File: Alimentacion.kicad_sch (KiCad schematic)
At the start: 0 parts

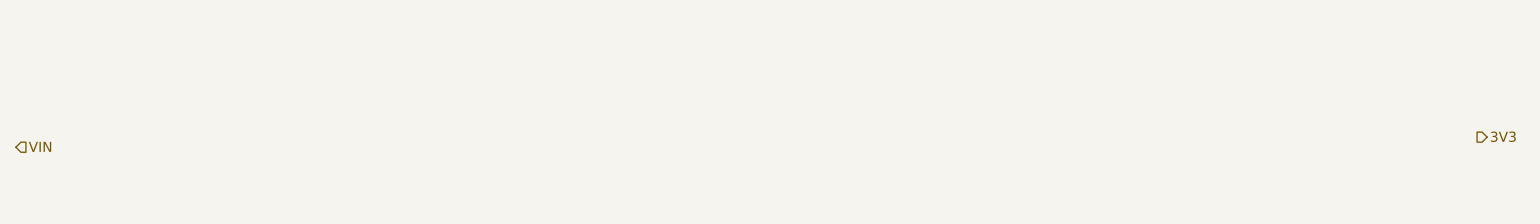
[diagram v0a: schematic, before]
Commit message: Alimentacion: J101 bornas 9 V, U201 MCP1703A 3,3 V, C201/C202 1 uF (huellas y MPN)
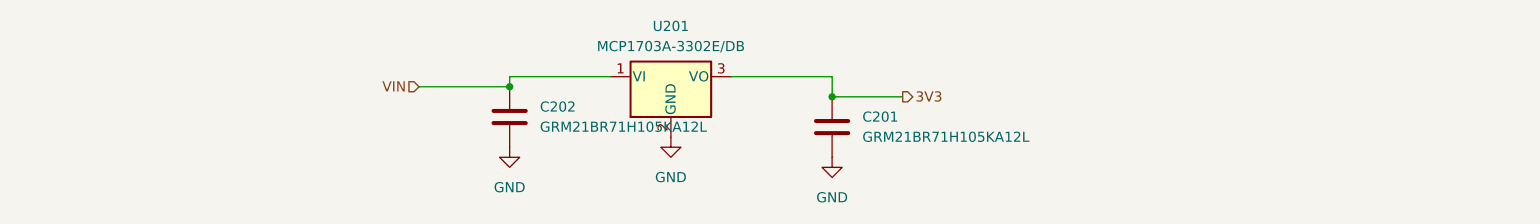
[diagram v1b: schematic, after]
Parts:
- added C201: GRM21BR71H105KA12L, Capacitor_SMD:C_0805_2012Metric_Pad1.18x1.45mm_HandSolder, symbol Device:C
- added C202: GRM21BR71H105KA12L, Package_TO_SOT_SMD:SOT-223-3_TabPin2, symbol Device:C
- added U201: MCP1703A-3302E/DB, Package_TO_SOT_SMD:SOT-223-3_TabPin2, symbol Regulator_Linear:MCP1703Ax-330xxDB
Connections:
- net 3V3: now also C201.1, U201.3 (VO)
- net VIN: now also C202.1, U201.1 (VI)
- new net GND: C201.2, C202.2, U201.2 (GND)

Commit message: Correcciones
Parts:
- C202: footprint Package_TO_SOT_SMD:SOT-223-3_TabPin2 -> Capacitor_SMD:C_0805_2012Metric_Pad1.18x1.45mm_HandSolder
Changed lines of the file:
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@@
 			)
 		)
-		(property "Footprint" "Package_TO_SOT_SMD:SOT-223-3_TabPin2"
+		(property "Footprint" "Capacitor_SMD:C_0805_2012Metric_Pad1.18x1.45mm_HandSolder"
 			(at 112.7252 101.6 0)
 			(hide yes)

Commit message: Correcciones: huella C202, conectores J301/J302, SWD al MCU, MPN en su campo y BOM
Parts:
- C201, C202: MPN (none) -> GRM21BR71H105KA12L; Manufacturer (none) -> Murata
- U201: MPN (none) -> MCP1703A-3302E/DB; Manufacturer (none) -> Microchip
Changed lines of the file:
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@@
 			)
 		)
-		(property "MPN" ""
+		(property "MPN" "MCP1703A-3302E/DB"
 			(at 132.08 92.71 0)
 			(hide yes)
@@
 			)
 		)
-		(property "Manufacturer" ""
+		(property "Manufacturer" "Microchip"
 			(at 132.08 92.71 0)
 			(hide yes)
@@
 			)
 		)
-		(property "MPN" ""
+		(property "MPN" "GRM21BR71H105KA12L"
 			(at 152.4 99.06 0)
 			(hide yes)
@@
 			)
 		)
-		(property "Manufacturer" ""
+		(property "Manufacturer" " Murata"
 			(at 152.4 99.06 0)
 			(hide yes)
@@
 			)
 		)
-		(property "MPN" ""
+		(property "MPN" "GRM21BR71H105KA12L"
 			(at 111.76 97.79 0)
 			(hide yes)
@@
 			)
 		)
-		(property "Manufacturer" ""
+		(property "Manufacturer" " Murata"
 			(at 111.76 97.79 0)
 			(hide yes)

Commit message: Valores eléctricos en Value y BOM actualizada
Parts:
- C201, C202: value GRM21BR71H105KA12L -> 1u
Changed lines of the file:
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@@
 			)
 		)
-		(property "Value" "GRM21BR71H105KA12L"
+		(property "Value" "1u"
 			(at 156.21 100.3299 0)
 			(show_name no)
@@
 			)
 		)
-		(property "Value" "GRM21BR71H105KA12L"
+		(property "Value" "1u"
 			(at 115.57 99.0599 0)
 			(show_name no)

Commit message: Esquema: desacoplo de U301 (100 nF + 4,7 uF) y puntos de test VIN/3V3/GND
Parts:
- added TP201, TP202, TP203: TestPoint, TestPoint:TestPoint_Keystone_5000-5004_Miniature, symbol Connector:TestPoint
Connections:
- net 3V3: now also TP202.1
- net GND: now also TP203.1
- net VIN: now also TP201.1
